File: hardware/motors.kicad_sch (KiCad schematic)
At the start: 12 parts, among them J2 Conn_01x02, J3 Conn_01x02, J4 Conn_01x02, U3 DRV8212, U4 DRV8212

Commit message: Updated values to be in standard series
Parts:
- C23: value 500uF -> 560uF
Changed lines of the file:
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@@
 			)
 		)
-		(property "Value" "500uF"
+		(property "Value" "560uF"
 			(at 127 81.6609 0)
 			(effects

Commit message: Updated decoupling caps
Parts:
- C23: value 560uF -> 270uF
- C24, C25: value 1000uF -> 680uF
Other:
- note added: "Bulk capacitance calculated with C_{bulk} > 3 * ∆I_{motor} / f_{PWM} / ∆V_{supply} Using f_{PWM} = 32 kHz, ∆V_{supply} = 0.05V Big motors: ∆I_{motor} = 0.04A Small motor: ∆I_{motor} = 0.02A With a bit of safety margin included"
- note added: "From https://www.ti.com/lit/an/slvaft0/slvaft0.pdf"
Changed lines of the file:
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@@
+		)
+	)
+	(text "Bulk capacitance calculated with C_{bulk} >  3 * ∆I_{motor} / f_{PWM} / ∆V_{supply}\nUsing f_{PWM} = 32 kHz, ∆V_{supply} = 0.05V\nBig motors:  ∆I_{motor} = 0.04A\nSmall motor: ∆I_{motor} = 0.02A\nWith a bit of safety margin included"
+		(exclude_from_sim no)
+		(at 77.978 32.258 0)
+		(effects
+			(font
+				(size 1.524 1.524)
+			)
+			(justify left)
+		)
+	)
+	(text "From https://www.ti.com/lit/an/slvaft0/slvaft0.pdf"
+		(exclude_from_sim no)
+		(at 100.584 42.672 0)
+		(effects
+			(font
+				(size 1.143 1.143)
+			)
 		)
 	)
@@
 			)
 		)
-		(property "Value" "560uF"
+		(property "Value" "270uF"
 			(at 127 81.6609 0)
 			(effects
@@
 			)
 		)
-		(property "Value" "1000uF"
+		(property "Value" "680uF"
 			(at 242.57 75.3109 0)
 			(effects
@@
 			)
 		)
-		(property "Value" "1000uF"
+		(property "Value" "680uF"
 			(at 230.378 83.82 0)
 			(effects

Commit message: Assigned footprints for connectors
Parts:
- J2: value Conn_01x02 -> JST_PH_01x02; footprint (none) -> Connector_JST:JST_PH_B2B-PH-K_1x02_P2.00mm_Vertical
- J3, J4: value Conn_01x02 -> JST_XH_01x02; footprint (none) -> Connector_JST:JST_XH_B2B-XH-A_1x02_P2.50mm_Vertical
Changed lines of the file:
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@@
 			)
 		)
-		(property "Value" "Conn_01x02"
+		(property "Value" "JST_XH_01x02"
 			(at 214.63 99.0599 0)
 			(effects
@@
 			)
 		)
-		(property "Footprint" ""
+		(property "Footprint" "Connector_JST:JST_XH_B2B-XH-A_1x02_P2.50mm_Vertical"
 			(at 212.09 96.52 0)
 			(effects
@@
 			)
 		)
-		(property "Value" "Conn_01x02"
+		(property "Value" "JST_XH_01x02"
 			(at 214.63 118.1099 0)
 			(effects
@@
 			)
 		)
-		(property "Footprint" ""
+		(property "Footprint" "Connector_JST:JST_XH_B2B-XH-A_1x02_P2.50mm_Vertical"
 			(at 212.09 115.57 0)
 			(effects
@@
 			)
 		)
-		(property "Value" "Conn_01x02"
+		(property "Value" "JST_PH_01x02"
 			(at 110.49 107.9499 0)
 			(effects
@@
 			)
 		)
-		(property "Footprint" ""
+		(property "Footprint" "Connector_JST:JST_PH_B2B-PH-K_1x02_P2.00mm_Vertical"
 			(at 107.95 105.41 0)
 			(effects

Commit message: Assigned footprints for capacitors and inductors
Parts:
- C15, C16, C17, C18: footprint (none) -> Capacitor_SMD:C_0603_1608Metric_Pad1.08x0.95mm_HandSolder
- C23: footprint (none) -> Capacitor_THT:CP_Radial_D6.3mm_P2.50mm
- C24, C25: footprint (none) -> Capacitor_THT:CP_Radial_D7.5mm_P2.50mm
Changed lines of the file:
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@@
 			)
 		)
-		(property "Footprint" ""
+		(property "Footprint" "Capacitor_SMD:C_0603_1608Metric_Pad1.08x0.95mm_HandSolder"
 			(at 220.0148 78.74 0)
 			(effects
@@
 			)
 		)
-		(property "Footprint" ""
+		(property "Footprint" "Capacitor_SMD:C_0603_1608Metric_Pad1.08x0.95mm_HandSolder"
 			(at 178.7652 91.44 0)
 			(effects
@@
 			)
 		)
-		(property "Footprint" ""
+		(property "Footprint" "Capacitor_THT:CP_Radial_D6.3mm_P2.50mm"
 			(at 124.1552 85.09 0)
 			(effects
@@
 			)
 		)
-		(property "Footprint" ""
+		(property "Footprint" "Capacitor_THT:CP_Radial_D7.5mm_P2.50mm"
 			(at 239.7252 78.74 0)
 			(effects
@@
 			)
 		)
-		(property "Footprint" ""
+		(property "Footprint" "Capacitor_SMD:C_0603_1608Metric_Pad1.08x0.95mm_HandSolder"
 			(at 74.6252 92.71 0)
 			(effects
@@
 			)
 		)
-		(property "Footprint" ""
+		(property "Footprint" "Capacitor_THT:CP_Radial_D7.5mm_P2.50mm"
 			(at 232.1052 78.74 0)
 			(effects
@@
 			)
 		)
-		(property "Footprint" ""
+		(property "Footprint" "Capacitor_SMD:C_0603_1608Metric_Pad1.08x0.95mm_HandSolder"
 			(at 114.6048 85.09 0)
 			(effects

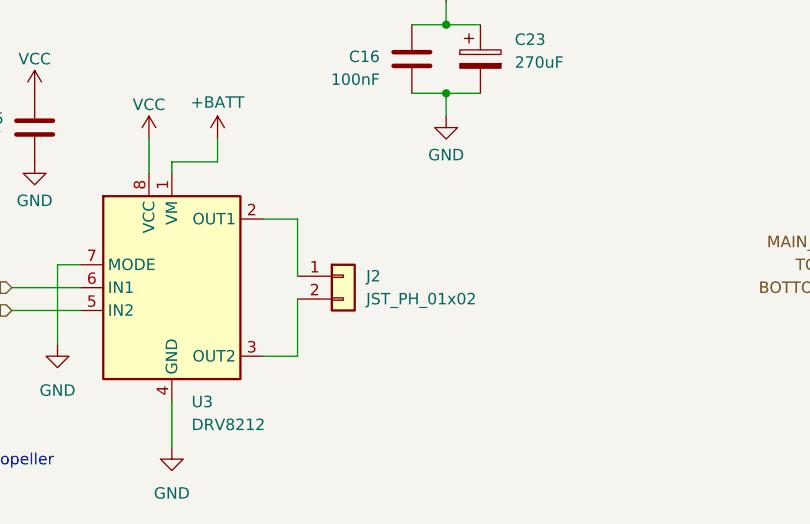
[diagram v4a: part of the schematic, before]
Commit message: Corrected pin order on JST connectors
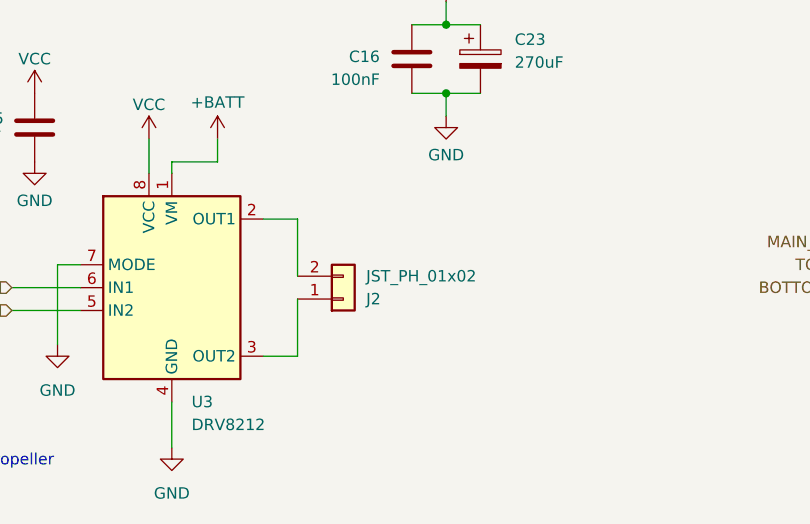
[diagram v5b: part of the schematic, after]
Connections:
- net at U3.2 (OUT1): now also J2.2 (Pin_2); no longer J2.1 (Pin_1)
- net at U3.3 (OUT2): now also J2.1 (Pin_1); no longer J2.2 (Pin_2)
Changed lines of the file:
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@@
 	(symbol
 		(lib_id "Connector_Generic:Conn_01x02")
-		(at 107.95 105.41 0)
+		(at 107.95 107.95 0)
+		(mirror x)
 		(unit 1)
 		(exclude_from_sim no)
@@
 		(on_board yes)
 		(dnp no)
-		(fields_autoplaced yes)
 		(property "Reference" "J2"
-			(at 110.49 105.4099 0)
+			(at 110.49 107.9501 0)
 			(effects
 				(font
@@
 		)
 		(property "Value" "JST_PH_01x02"
-			(at 110.49 107.9499 0)
+			(at 110.49 105.4101 0)
 			(effects
 				(font
@@
 		)
 		(property "Footprint" "Connector_JST:JST_PH_B2B-PH-K_1x02_P2.00mm_Vertical"
-			(at 107.95 105.41 0)
+			(at 107.95 107.95 0)
 			(effects
 				(font
@@
 		)
 		(property "Datasheet" "~"
-			(at 107.95 105.41 0)
+			(at 107.95 107.95 0)
 			(effects
 				(font
@@
 		)
 		(property "Description" "Generic connector, single row, 01x02, script generated (kicad-library-utils/schlib/autogen/connector/)"
-			(at 107.95 105.41 0)
+			(at 107.95 107.95 0)
 			(effects
 				(font

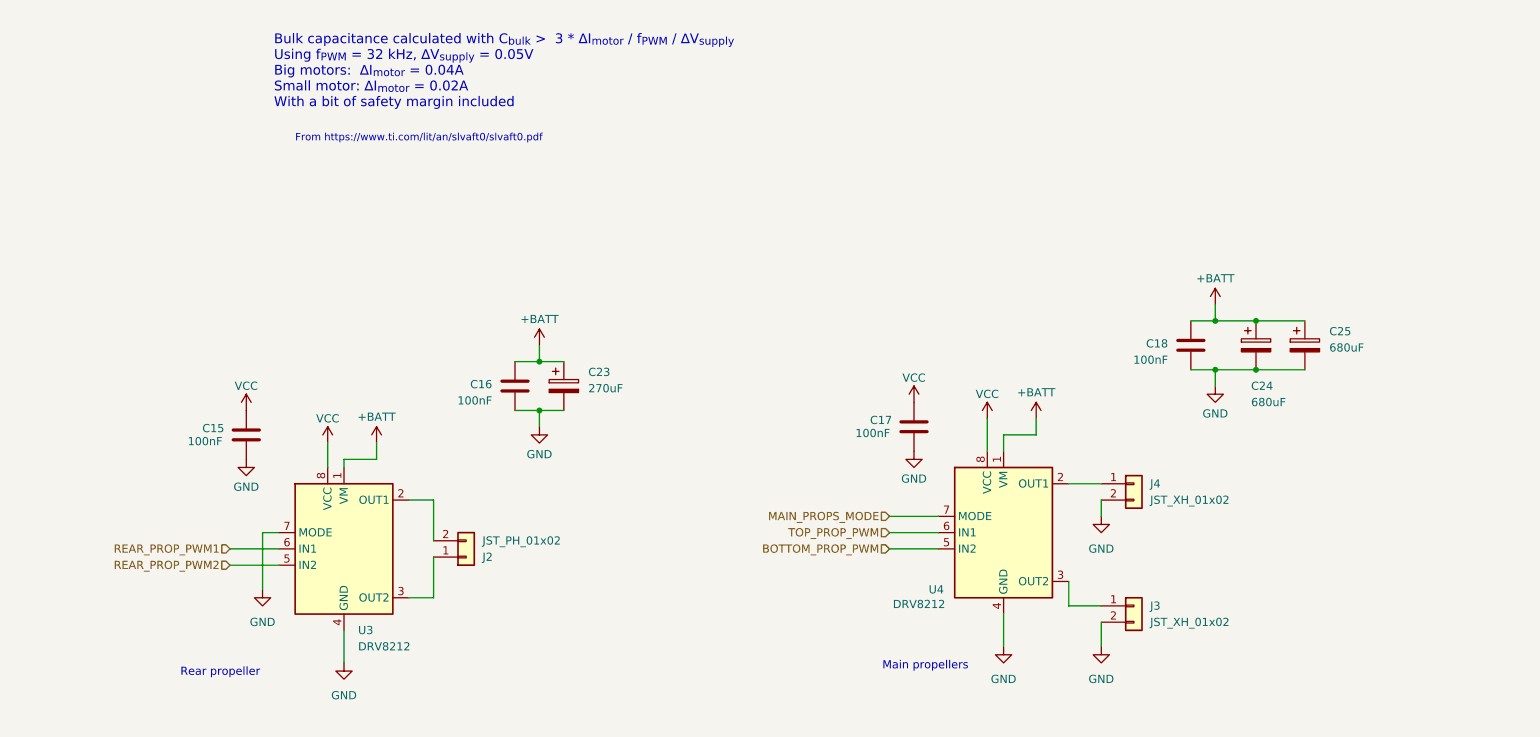
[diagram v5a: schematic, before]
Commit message: Updated decoupling caps to match guidelines from Eric Bogatin
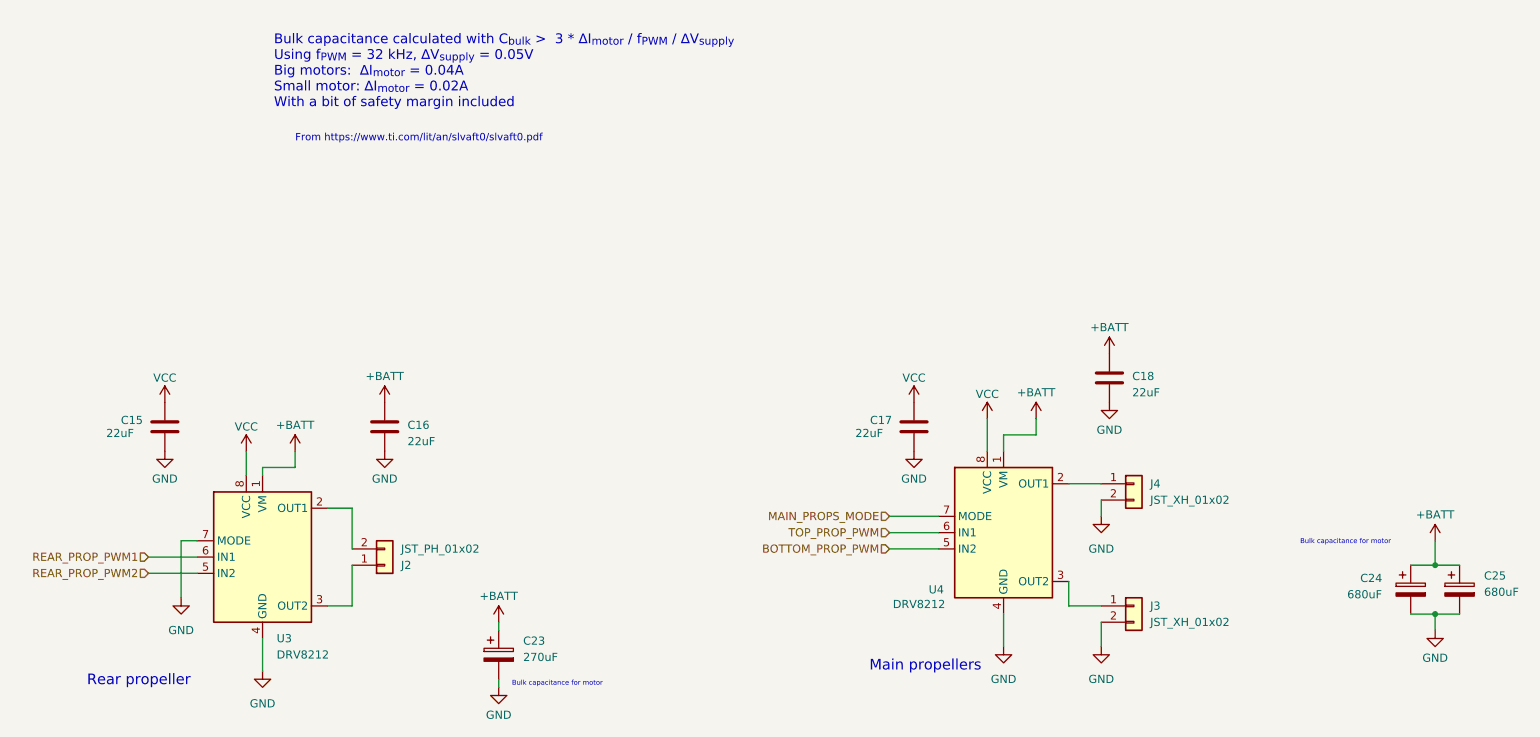
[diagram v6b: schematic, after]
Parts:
- C15, C16, C17, C18: value 100nF -> 22uF
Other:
- note added: "Bulk capacitance for motor"
- moved on the sheet: C15, C23, C24, C25, J2, U3

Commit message: New layout idea, savepoint
Me reckons this is the way to go. Only 1 motor bulk capacitor
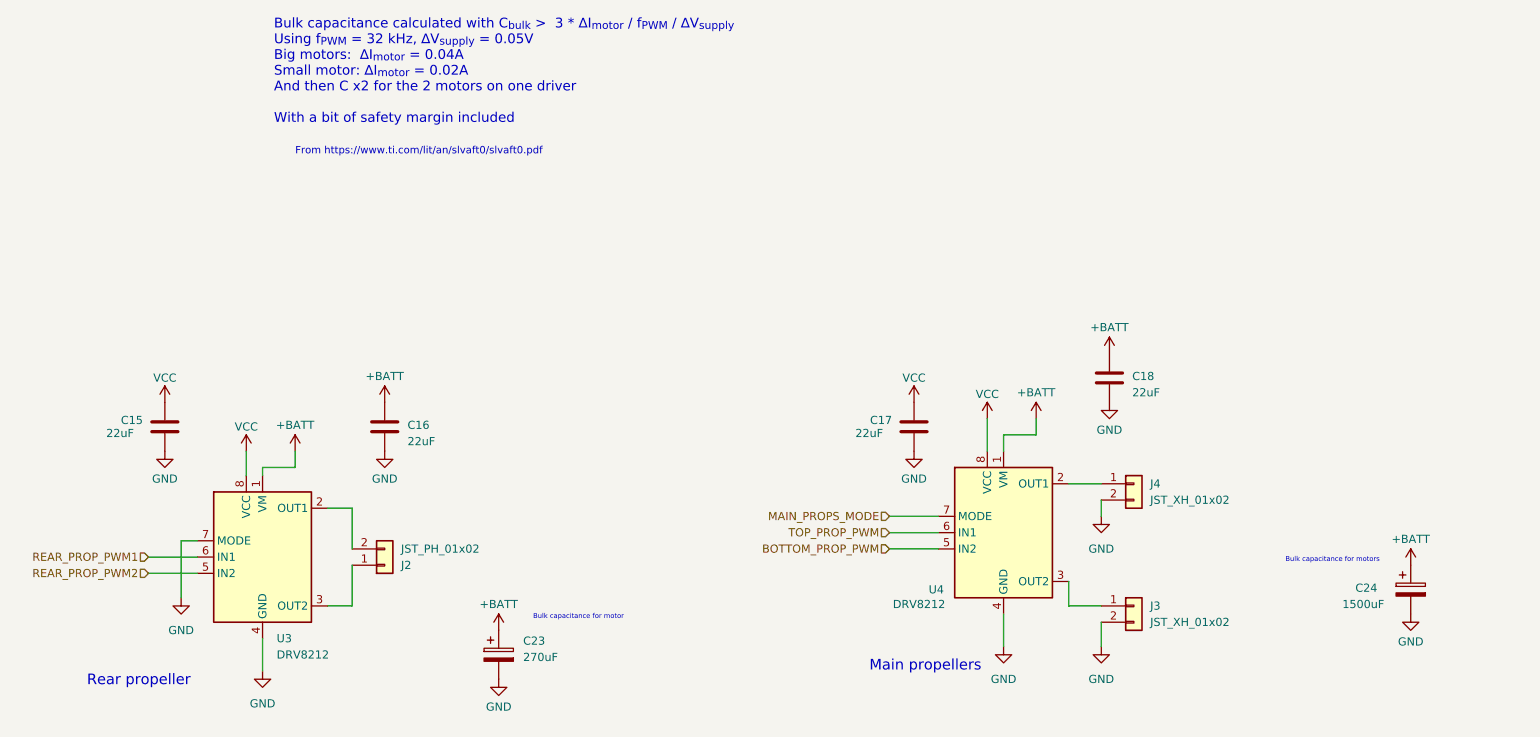
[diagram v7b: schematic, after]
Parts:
- removed C25: 680uF, Capacitor_THT:CP_Radial_D7.5mm_P2.50mm, symbol Device:C_Polarized
- C24: value 680uF -> 1500uF; footprint Capacitor_THT:CP_Radial_D7.5mm_P2.50mm -> Capacitor_THT:CP_Radial_D10.0mm_P5.00mm
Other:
- note added: "Bulk capacitance calculated with C_{bulk} > 3 * ∆I_{motor} / f_{PWM} / ∆V_{supply} Using f_{PWM} = 32 kHz, ∆V_{supply} = 0.05V Big motors: ∆I_{motor} = 0.04A Small motor: ∆I_{motor} = 0.02A And then C x2 for the 2 motors on one driver With a bit of safety margin included"
- note added: "Bulk capacitance for motors"
- note removed: "Bulk capacitance calculated with C_{bulk} > 3 * ∆I_{motor} / f_{PWM} / ∆V_{supply} Using f_{PWM} = 32 kHz, ∆V_{supply} = 0.05V Big motors: ∆I_{motor} = 0.04A Small motor: ∆I_{motor} = 0.02A With a bit of safety margin included"
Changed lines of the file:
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@@
 	(generator_version "8.0")
 	(paper "A4")
-	(junction
-		(at 259.08 109.22)
-		(diameter 0)
-		(color 0 0 0 0)
-	)
-	(junction
-		(at 259.08 116.84)
-		(diameter 0)
-		(color 0 0 0 0)
-	)
 	(wire
 		(pts
@@
 	(wire
 		(pts
-			(xy 259.08 105.41) (xy 259.08 109.22)
-		)
-		(stroke
-			(width 0)
-			(type default)
-		)
-	)
-	(wire
-		(pts
 			(xy 66.04 105.41) (xy 63.5 105.41)
 		)
@@
 	(wire
 		(pts
-			(xy 255.27 109.22) (xy 259.08 109.22)
-		)
-		(stroke
-			(width 0)
-			(type default)
-		)
-	)
-	(wire
-		(pts
 			(xy 58.42 110.49) (xy 66.04 110.49)
 		)
@@
 	(wire
 		(pts
-			(xy 259.08 119.38) (xy 259.08 116.84)
-		)
-		(stroke
-			(width 0)
-			(type default)
-		)
-	)
-	(wire
-		(pts
 			(xy 63.5 105.41) (xy 63.5 114.3)
 		)
@@
 	(wire
 		(pts
-			(xy 259.08 116.84) (xy 262.89 116.84)
-		)
-		(stroke
-			(width 0)
-			(type default)
-		)
-	)
-	(wire
-		(pts
-			(xy 259.08 109.22) (xy 262.89 109.22)
-		)
-		(stroke
-			(width 0)
-			(type default)
-		)
-	)
-	(wire
-		(pts
-			(xy 259.08 116.84) (xy 255.27 116.84)
-		)
-		(stroke
-			(width 0)
-			(type default)
-		)
-	)
-	(wire
-		(pts
 			(xy 86.36 115.57) (xy 90.17 115.57)
 		)
@@
 	(wire
 		(pts
-			(xy 113.03 118.11) (xy 113.03 119.38)
-		)
-		(stroke
-			(width 0)
-			(type default)
-		)
-	)
-	(wire
-		(pts
 			(xy 201.93 96.52) (xy 207.01 96.52)
 		)
@@
 		(pts
 			(xy 189.23 86.36) (xy 189.23 91.44)
-		)
-		(stroke
-			(width 0)
-			(type default)
-		)
-	)
-	(wire
-		(pts
-			(xy 113.03 128.27) (xy 113.03 127)
 		)
 		(stroke
@@
 		)
 	)
-	(text "Bulk capacitance calculated with C_{bulk} >  3 * ∆I_{motor} / f_{PWM} / ∆V_{supply}\nUsing f_{PWM} = 32 kHz, ∆V_{supply} = 0.05V\nBig motors:  ∆I_{motor} = 0.04A\nSmall motor: ∆I_{motor} = 0.02A\nWith a bit of safety margin included"
+	(text "Bulk capacitance calculated with C_{bulk} >  3 * ∆I_{motor} / f_{PWM} / ∆V_{supply}\nUsing f_{PWM} = 32 kHz, ∆V_{supply} = 0.05V\nBig motors:  ∆I_{motor} = 0.04A\nSmall motor: ∆I_{motor} = 0.02A\nAnd then C x2 for the 2 motors on one driver\n\nWith a bit of safety margin included"
 		(exclude_from_sim no)
 		(at 77.978 32.258 0)
@@
 	(text "From https://www.ti.com/lit/an/slvaft0/slvaft0.pdf"
 		(exclude_from_sim no)
-		(at 100.584 42.672 0)
+		(at 100.584 44.704 0)
 		(effects
 			(font
@@
 	(text "Bulk capacitance for motor"
 		(exclude_from_sim no)
-		(at 122.174 127.762 0)
+		(at 125.476 117.348 0)
 		(effects
 			(font
@@
 		)
 	)
-	(text "Bulk capacitance for motor"
-		(exclude_from_sim no)
-		(at 245.11 105.664 0)
+	(text "Bulk capacitance for motors"
+		(exclude_from_sim no)
+		(at 243.078 108.458 0)
 		(effects
 			(font
@@
 	(symbol
 		(lib_id "power:GND")
-		(at 113.03 128.27 0)
+		(at 113.03 127 0)
 		(unit 1)
 		(exclude_from_sim no)
@@
 		(dnp no)
 		(property "Reference" "#PWR026"
-			(at 113.03 134.62 0)
+			(at 113.03 133.35 0)
 			(effects
 				(font
@@
 		)
 		(property "Value" "GND"
-			(at 113.03 132.588 0)
+			(at 113.03 131.318 0)
 			(effects
 				(font
@@
 		)
 		(property "Footprint" ""
-			(at 113.03 128.27 0)
+			(at 113.03 127 0)
 			(effects
 				(font
@@
 		)
 		(property "Datasheet" ""
-			(at 113.03 128.27 0)
+			(at 113.03 127 0)
 			(effects
 				(font
@@
 		)
 		(property "Description" "Power symbol creates a global label with name \"GND\" , ground"
-			(at 113.03 128.27 0)
+			(at 113.03 127 0)
 			(effects
 				(font
@@
 	(symbol
 		(lib_id "power:+BATT")
-		(at 259.08 105.41 0)
+		(at 255.27 109.22 0)
 		(unit 1)
 		(exclude_from_sim no)
@@
 		(dnp no)
 		(property "Reference" "#PWR031"
-			(at 259.08 109.22 0)
+			(at 255.27 113.03 0)
 			(effects
 				(font
@@
 		)
 		(property "Value" "+BATT"
-			(at 259.08 101.346 0)
+			(at 255.27 105.156 0)
 			(effects
 				(font
@@
 		)
 		(property "Footprint" ""
-			(at 259.08 105.41 0)
+			(at 255.27 109.22 0)
 			(effects
 				(font
@@
 		)
 		(property "Datasheet" ""
-			(at 259.08 105.41 0)
+			(at 255.27 109.22 0)
 			(effects
 				(font
@@
 		)
 		(property "Description" "Power symbol creates a global label with name \"+BATT\""
-			(at 259.08 105.41 0)
+			(at 255.27 109.22 0)
 			(effects
 				(font
@@
 	)
 	(symbol
-		(lib_id "Device:C_Polarized")
-		(at 262.89 113.03 0)
-		(unit 1)
-		(exclude_from_sim no)
-		(in_bom yes)
-		(on_board yes)
-		(dnp no)
-		(fields_autoplaced yes)
-		(property "Reference" "C25"
-			(at 266.7 110.8709 0)
-			(effects
-				(font
-					(size 1.27 1.27)
-				)
-				(justify left)
-			)
-		)
-		(property "Value" "680uF"
-			(at 266.7 113.4109 0)
-			(effects
-				(font
-					(size 1.27 1.27)
-				)
-				(justify left)
-			)
-		)
-		(property "Footprint" "Capacitor_THT:CP_Radial_D7.5mm_P2.50mm"
-			(at 263.8552 116.84 0)
-			(effects
-				(font
-					(size 1.27 1.27)
-				)
-				(hide yes)
-			)
-		)
-		(property "Datasheet" "~"
-			(at 262.89 113.03 0)
-			(effects
-				(font
-					(size 1.27 1.27)
-				)
-				(hide yes)
-			)
-		)
-		(property "Description" "Polarized capacitor"
-			(at 262.89 113.03 0)
-			(effects
-				(font
-					(size 1.27 1.27)
-				)
-				(hide yes)
-			)
-		)
-		(pin "2"
-		)
-		(pin "1"
-		)
-		(instances
-			(project "heli_avionics"
-				(path "/c384ea46-0dfb-4673-b2f4-1f88fafbcaa5/e66d27d0-3506-42a3-bb0e-923c7c751e41"
-					(reference "C25")
-					(unit 1)
-				)
-			)
-		)
-	)
-	(symbol
 		(lib_id "power:+BATT")
 		(at 196.85 86.36 0)
@@
 		(dnp no)
 		(property "Reference" "C24"
-			(at 247.396 111.252 0)
+			(at 246.634 112.776 0)
 			(effects
 				(font
@@
 			)
 		)
-		(property "Value" "680uF"
-			(at 245.364 113.792 0)
+		(property "Value" "1500uF"
+			(at 244.602 115.316 0)
 			(effects
 				(font
@@
 			)
 		)
-		(property "Footprint" "Capacitor_THT:CP_Radial_D7.5mm_P2.50mm"
+		(property "Footprint" "Capacitor_THT:CP_Radial_D10.0mm_P5.00mm"
 			(at 256.2352 116.84 0)
 			(effects
@@
 	(symbol
 		(lib_id "power:+BATT")
-		(at 113.03 118.11 0)
+		(at 113.03 119.38 0)
 		(unit 1)
 		(exclude_from_sim no)
@@
 		(dnp no)
 		(property "Reference" "#PWR025"
-			(at 113.03 121.92 0)
+			(at 113.03 123.19 0)
 			(effects
 				(font
@@
 		)
 		(property "Value" "+BATT"
-			(at 113.03 114.046 0)
+			(at 113.03 115.316 0)
 			(effects
 				(font
@@
 		)
 		(property "Footprint" ""
-			(at 113.03 118.11 0)
+			(at 113.03 119.38 0)
 			(effects
 				(font
@@
 		)
 		(property "Datasheet" ""
-			(at 113.03 118.11 0)
+			(at 113.03 119.38 0)
 			(effects
 				(font
@@
 		)
 		(property "Description" "Power symbol creates a global label with name \"+BATT\""
-			(at 113.03 118.11 0)
+			(at 113.03 119.38 0)
 			(effects
 				(font
@@
 	(symbol
 		(lib_id "power:GND")
-		(at 259.08 119.38 0)
+		(at 255.27 116.84 0)
 		(unit 1)
 		(exclude_from_sim no)
@@
 		(dnp no)
 		(property "Reference" "#PWR032"
-			(at 259.08 125.73 0)
+			(at 255.27 123.19 0)
 			(effects
 				(font
@@
 		)
 		(property "Value" "GND"
-			(at 259.08 123.698 0)
+			(at 255.27 121.158 0)
 			(effects
 				(font
@@
 		)
 		(property "Footprint" ""
-			(at 259.08 119.38 0)
+			(at 255.27 116.84 0)
 			(effects
 				(font
@@
 		)
 		(property "Datasheet" ""
-			(at 259.08 119.38 0)
+			(at 255.27 116.84 0)
 			(effects
 				(font
@@
 		)
 		(property "Description" "Power symbol creates a global label with name \"GND\" , ground"
-			(at 259.08 119.38 0)
-			(effects
-				(font
+			(at 255.27 116.84 0)
+			(effects
+				(font
